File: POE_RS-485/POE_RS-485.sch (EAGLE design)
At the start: 9 parts, among them IC1 7805

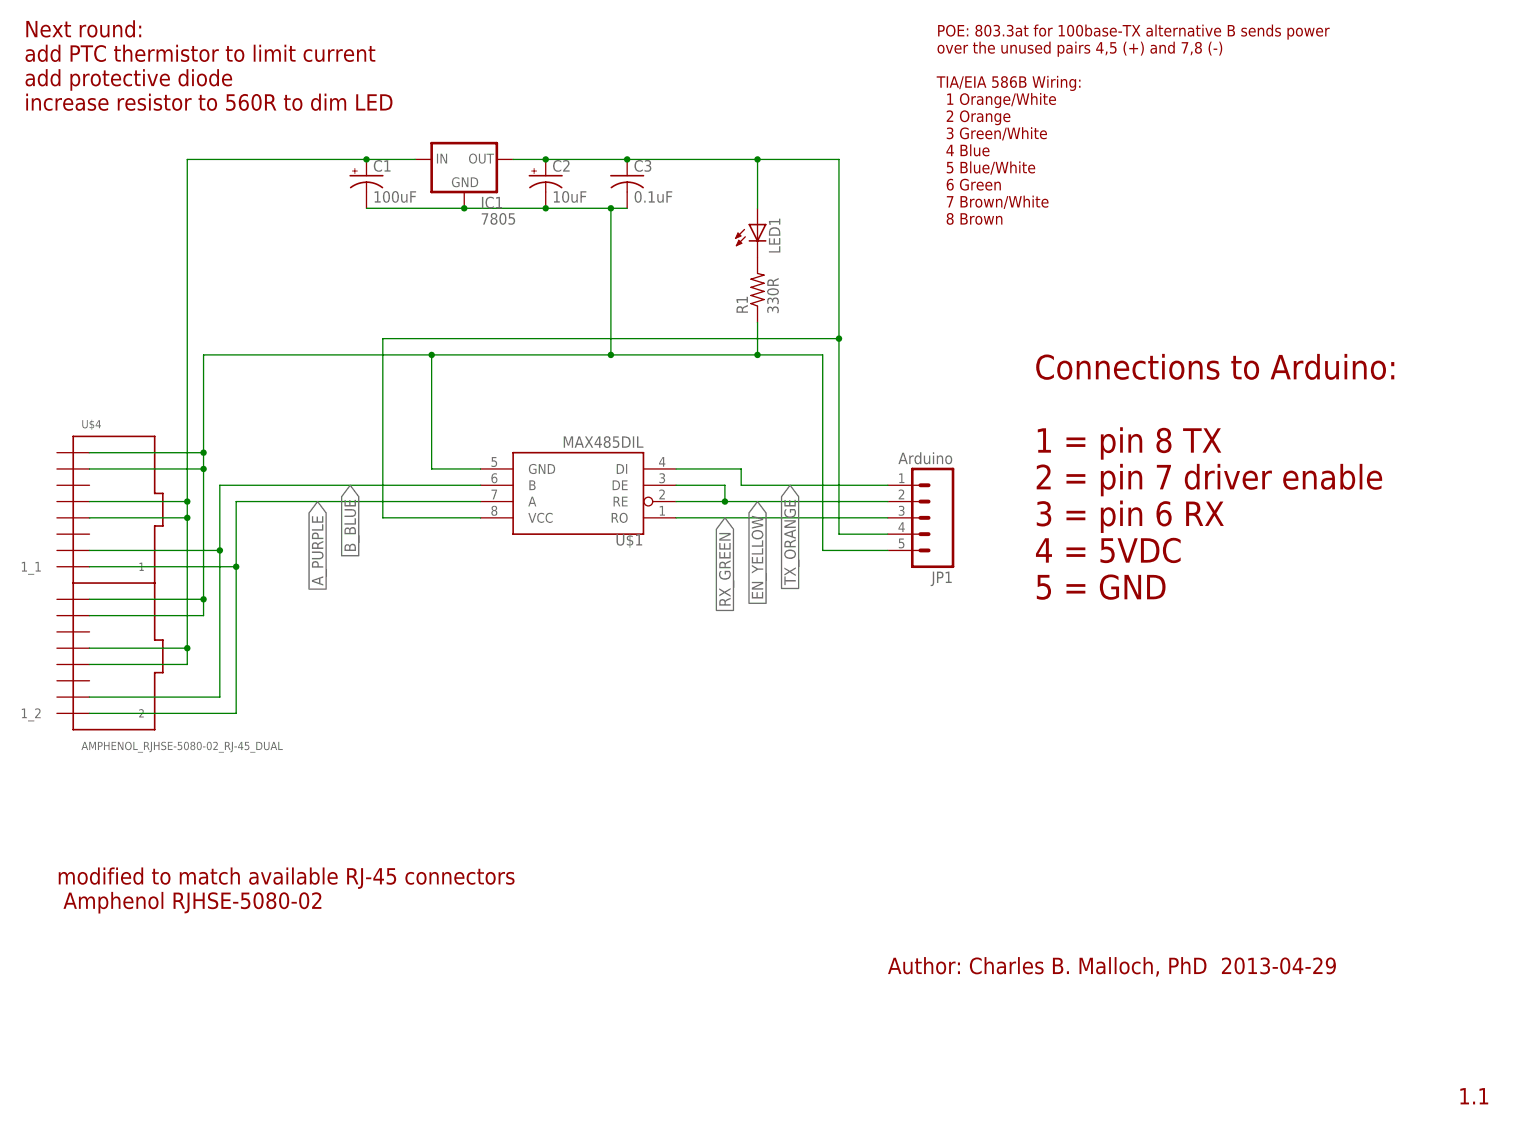
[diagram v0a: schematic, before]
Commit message: Hot tub fill monitor: added
other updates
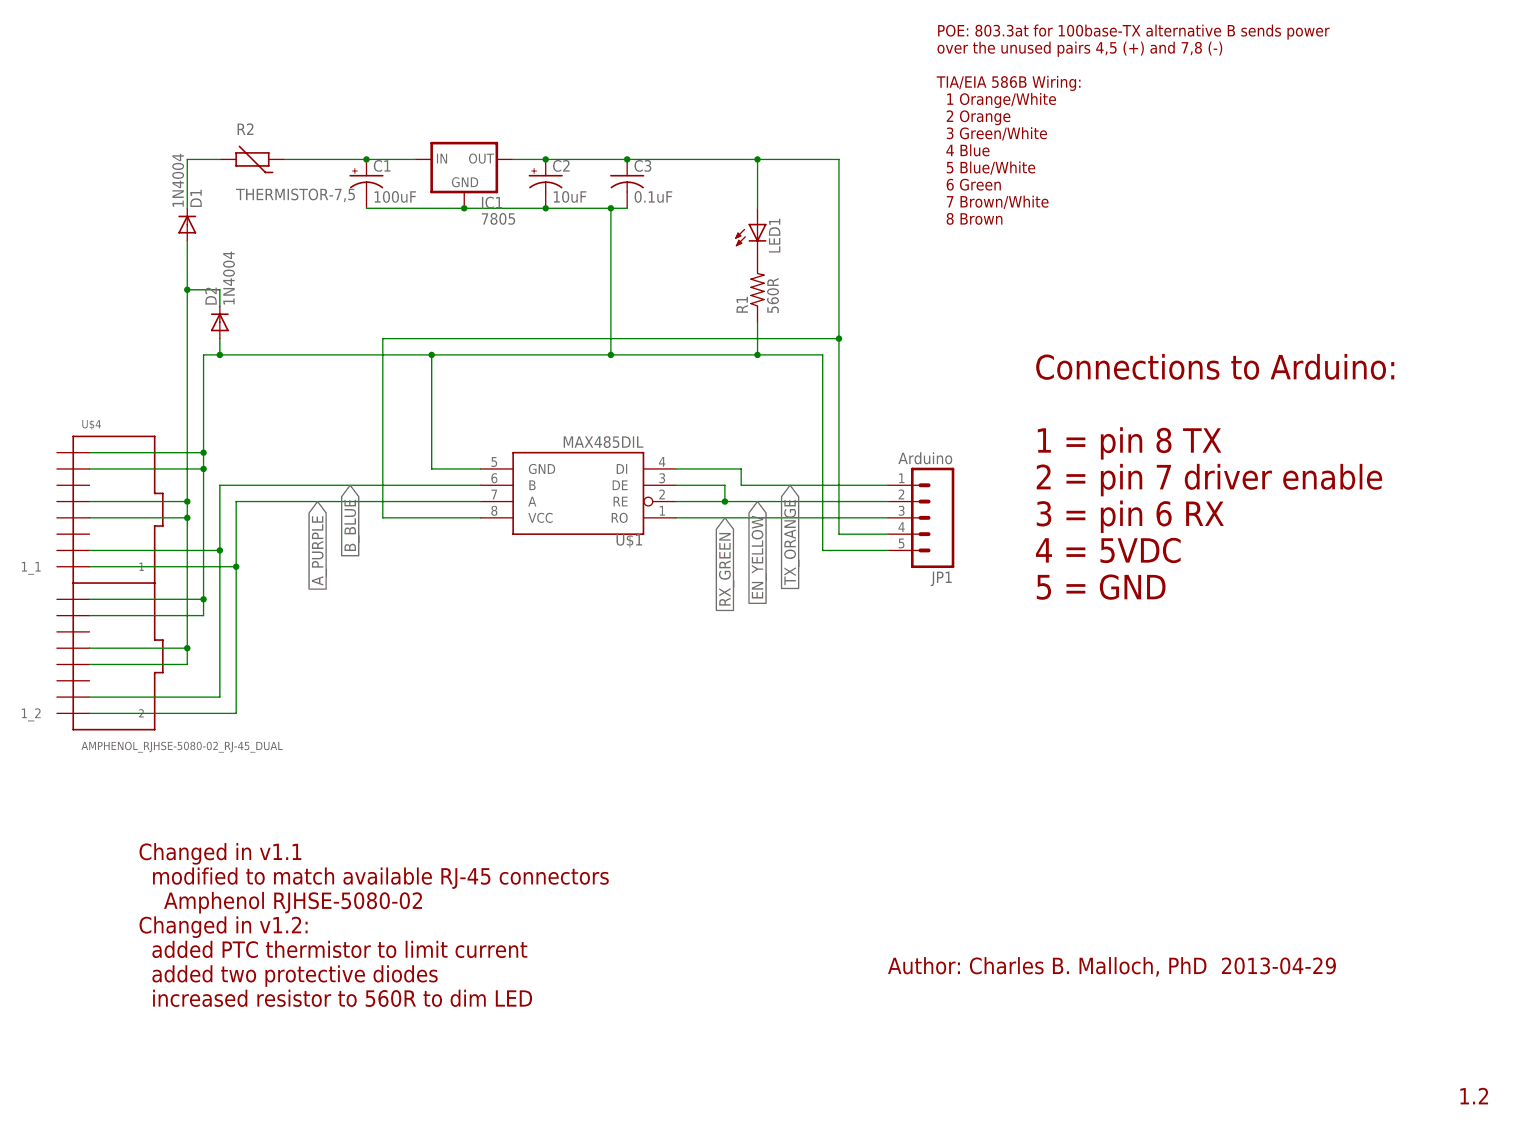
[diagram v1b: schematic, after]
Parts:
- added D1, D2: 1N4004, diode:1N4004
- added R2: THERMISTOR-7,5, varistor:THERMISTOR-7,5
- R1: value 330R -> 560R
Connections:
- new net N$3: C1.+, IC1.IN, R2.1
- new net N$4: D1.C, R2.2
- net GND: now also D2.A
- net VIN: now also D1.A, D2.C; no longer C1.+, IC1.IN
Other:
- note added: "1.2"
- note added: "Changed in v1.1 modified to match available RJ-45 connectors Amphenol RJHSE-5080-02 Changed in v1.2: added PTC thermistor to limit current added two protective diodes increased resistor to 560R to dim LED"
- note removed: "1.1"
- note removed: "Next round: add PTC thermistor to limit current add protective diode increase resistor to 560R to dim LED"
- note removed: "modified to match available RJ-45 connectors Amphenol RJHSE-5080-02"
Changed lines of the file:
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@@
 <?xml version="1.0" encoding="utf-8"?>
 <!DOCTYPE eagle SYSTEM "eagle.dtd">
-<eagle version="6.4">
+<eagle version="6.5.0">
 <drawing>
 <settings>
@@
 <part name="C3" library="adafruit" deviceset="C-US" device="025-025X050" value="0.1uF"/>
 <part name="JP1" library="SparkFun-Connectors" deviceset="M05" device="LOCK_LONGPADS" value="Arduino"/>
-<part name="R1" library="resistor" deviceset="R-US_" device="0204/7" value="330R"/>
+<part name="R1" library="resistor" deviceset="R-US_" device="0204/7" value="560R"/>
 <part name="LED1" library="led" deviceset="LED" device="3MM"/>
 <part name="U$4" library="cbm_parts" deviceset="AMPHENOL_RJHSE-5080-02_RJ-45_DUAL" device=""/>
+<part name="R2" library="varistor" deviceset="THERMISTOR" device="-7,5"/>
+<part name="D1" library="diode" deviceset="1N4004" device=""/>
+<part name="D2" library="diode" deviceset="1N4004" device=""/>
 </parts>
 <sheets>
@@
 <plain>
 <text x="139.7" y="17.78" size="2.54" layer="94">Author: Charles B. Malloch, PhD  2013-04-29</text>
-<text x="228.6" y="-2.54" size="2.54" layer="94">1.1</text>
+<text x="228.6" y="-2.54" size="2.54" layer="94">1.2</text>
 <text x="162.56" y="76.2" size="3.81" layer="94">Connections to Arduino:
 1 = pin 8 TX
@@
   7 Brown/White
   8 Brown</text>
-<text x="10.16" y="27.94" size="2.54" layer="94">modified to match available RJ-45 connectors
- Amphenol RJHSE-5080-02</text>
-<text x="5.08" y="152.4" size="2.54" layer="94">Next round:
-add PTC thermistor to limit current
-add protective diode
-increase resistor to 560R to dim LED</text>
+<text x="22.86" y="12.7" size="2.54" layer="94">Changed in v1.1
+  modified to match available RJ-45 connectors
+    Amphenol RJHSE-5080-02
+Changed in v1.2:
+  added PTC thermistor to limit current
+  added two protective diodes
+  increased resistor to 560R to dim LED</text>
 </plain>
 <instances>
@@
 <instance part="LED1" gate="G$1" x="119.38" y="134.62"/>
 <instance part="U$4" gate="G$1" x="20.32" y="78.74"/>
+<instance part="R2" gate="G$1" x="40.64" y="144.78"/>
+<instance part="D1" gate="1" x="30.48" y="134.62" rot="MR90"/>
+<instance part="D2" gate="1" x="35.56" y="119.38" rot="R90"/>
 </instances>
 <busses>
@@
 <wire x1="68.58" y1="96.52" x2="76.2" y2="96.52" width="0.1524" layer="91"/>
 <wire x1="68.58" y1="96.52" x2="68.58" y2="114.3" width="0.1524" layer="91"/>
-<wire x1="68.58" y1="114.3" x2="33.02" y2="114.3" width="0.1524" layer="91"/>
+<wire x1="68.58" y1="114.3" x2="35.56" y2="114.3" width="0.1524" layer="91"/>
 <pinref part="C1" gate="G$1" pin="-"/>
 <pinref part="IC1" gate="G$1" pin="GND"/>
 <pinref part="C2" gate="G$1" pin="-"/>
 <pinref part="C3" gate="G$1" pin="2"/>
+<wire x1="35.56" y1="114.3" x2="33.02" y2="114.3" width="0.1524" layer="91"/>
 <wire x1="99.06" y1="137.16" x2="96.52" y2="137.16" width="0.1524" layer="91"/>
 <junction x="86.36" y="137.16"/>
@@
 <pinref part="U$4" gate="G$1" pin="7_2"/>
 <wire x1="15.24" y1="73.66" x2="33.02" y2="73.66" width="0.1524" layer="91"/>
+<pinref part="D2" gate="1" pin="A"/>
+<wire x1="35.56" y1="116.84" x2="35.56" y2="114.3" width="0.1524" layer="91"/>
+<junction x="35.56" y="114.3"/>
 </segment>
 </net>
@@
 <net name="VIN" class="1">
 <segment>
-<pinref part="C1" gate="G$1" pin="+"/>
 <wire x1="30.48" y1="66.04" x2="30.48" y2="68.58" width="0.1524" layer="91"/>
 <wire x1="30.48" y1="68.58" x2="30.48" y2="88.9" width="0.1524" layer="91"/>
 <wire x1="30.48" y1="88.9" x2="30.48" y2="91.44" width="0.1524" layer="91"/>
-<wire x1="30.48" y1="91.44" x2="30.48" y2="144.78" width="0.1524" layer="91"/>
-<wire x1="30.48" y1="144.78" x2="58.42" y2="144.78" width="0.1524" layer="91"/>
-<pinref part="IC1" gate="G$1" pin="IN"/>
-<wire x1="58.42" y1="144.78" x2="66.04" y2="144.78" width="0.1524" layer="91"/>
-<junction x="58.42" y="144.78"/>
 <junction x="30.48" y="88.9"/>
 <wire x1="15.24" y1="88.9" x2="30.48" y2="88.9" width="0.1524" layer="91"/>
-<junction x="30.48" y="91.44"/>
 <wire x1="15.24" y1="91.44" x2="30.48" y2="91.44" width="0.1524" layer="91"/>
 <junction x="30.48" y="68.58"/>
@@
 <pinref part="U$4" gate="G$1" pin="4_2"/>
 <wire x1="15.24" y1="66.04" x2="30.48" y2="66.04" width="0.1524" layer="91"/>
+<wire x1="30.48" y1="91.44" x2="30.48" y2="124.46" width="0.1524" layer="91"/>
+<junction x="30.48" y="91.44"/>
+<pinref part="D1" gate="1" pin="A"/>
+<pinref part="D2" gate="1" pin="C"/>
+<wire x1="30.48" y1="124.46" x2="30.48" y2="132.08" width="0.1524" layer="91"/>
+<wire x1="35.56" y1="121.92" x2="35.56" y2="124.46" width="0.1524" layer="91"/>
+<wire x1="35.56" y1="124.46" x2="30.48" y2="124.46" width="0.1524" layer="91"/>
+<junction x="30.48" y="124.46"/>
 </segment>
 </net>
@@
 </segment>
 </net>
+<net name="N$3" class="1">
+<segment>
+<pinref part="IC1" gate="G$1" pin="IN"/>
+<pinref part="C1" gate="G$1" pin="+"/>
+<wire x1="58.42" y1="144.78" x2="66.04" y2="144.78" width="0.1524" layer="91"/>
+<junction x="58.42" y="144.78"/>
+<pinref part="R2" gate="G$1" pin="1"/>
+<wire x1="45.72" y1="144.78" x2="58.42" y2="144.78" width="0.1524" layer="91"/>
+</segment>
+</net>
+<net name="N$4" class="1">
+<segment>
+<pinref part="R2" gate="G$1" pin="2"/>
+<wire x1="30.48" y1="144.78" x2="35.56" y2="144.78" width="0.1524" layer="91"/>
+<pinref part="D1" gate="1" pin="C"/>
+<wire x1="30.48" y1="137.16" x2="30.48" y2="144.78" width="0.1524" layer="91"/>
+</segment>
+</net>
